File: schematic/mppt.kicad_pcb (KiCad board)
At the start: 2 copper layers, 22 parts, among them J1 Solar, J10 ACS712-OUT, J11 LiIon-36V, J12 Download, J2 TL494-IN, J3 LM2596-IN, J4 LM2596-IN, J5 Serial, J6 LM2596-OUT-4,5V, J7 LM2596-OUT-3,3V, J8 ACS712-IN, J9 TL494-OUT-42V-3A, U3 ESP-03, U4 74HC4051

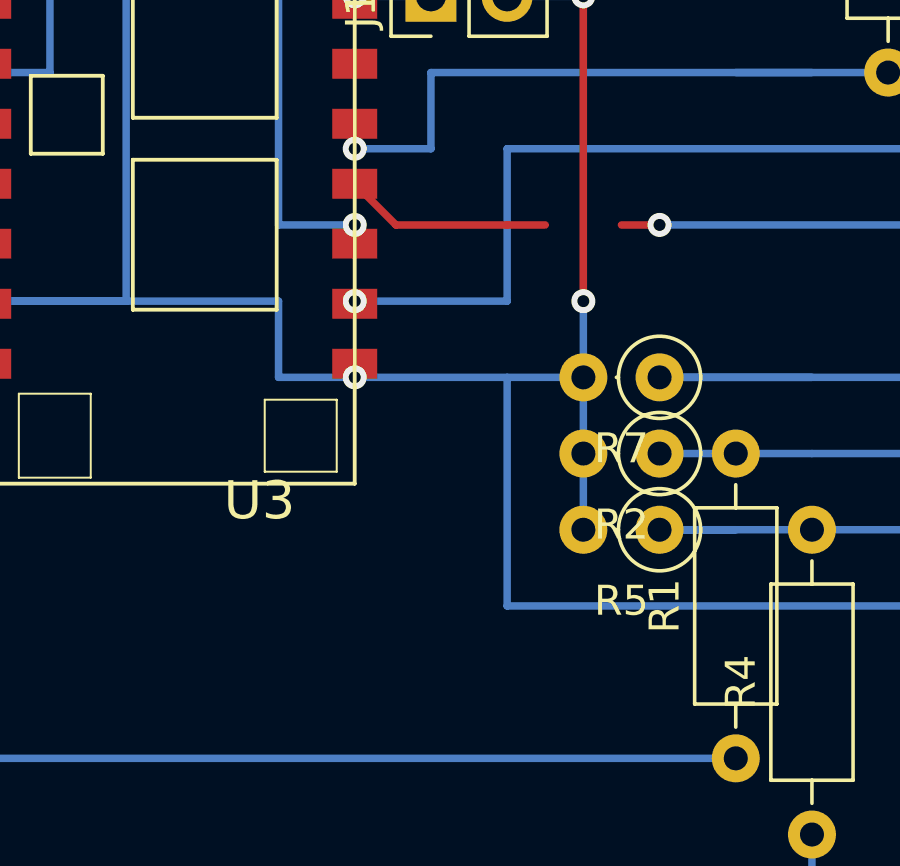
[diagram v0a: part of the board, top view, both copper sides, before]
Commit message: schematic: Use rsistor for DTC connection to limit current to TL494 capacitor
Signed-off-by: Timo Wischer <twischer@freenet.de>
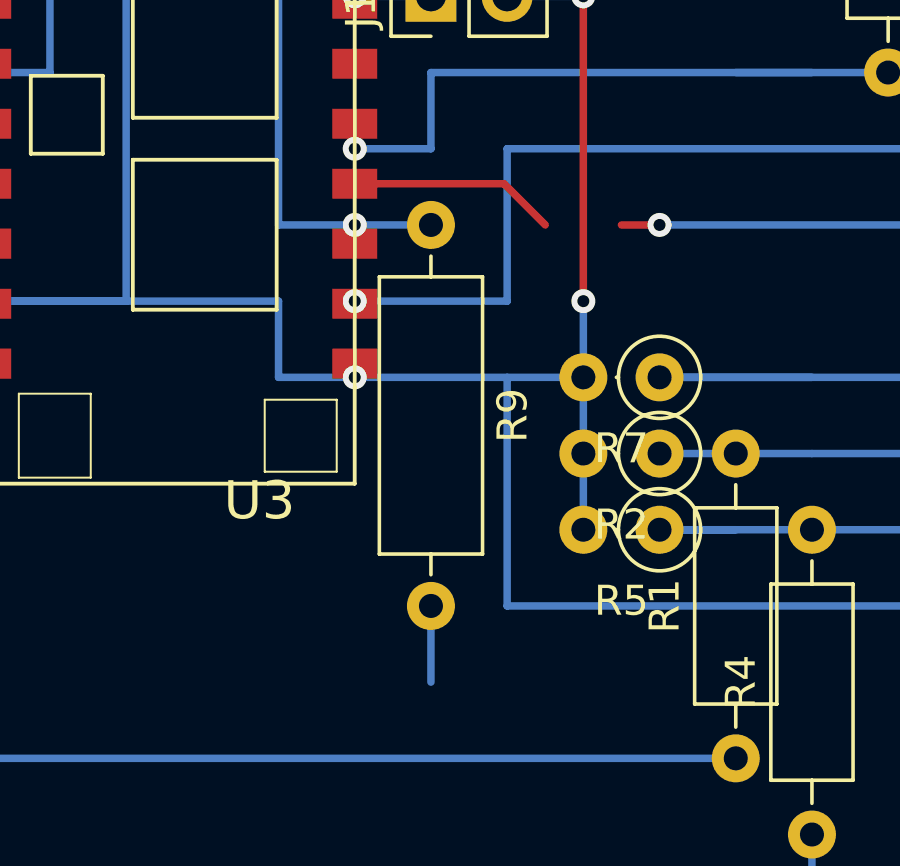
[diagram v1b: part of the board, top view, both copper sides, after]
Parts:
- added R9: 1k2, Resistor_THT:R_Axial_DIN0309_L9.0mm_D3.2mm_P12.70mm_Horizontal, F.Cu at (81.3, 127.0)
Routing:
- net (no net): track 0.00 -> 2.54 mm
- net Net-(D1-Pad1): track 18.4 -> 20.9 mm
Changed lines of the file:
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@@
     (thickness 1.6)
     (drawings 0)
-    (tracks 124)
+    (tracks 125)
     (zones 0)
-    (modules 22)
+    (modules 23)
     (nets 20)
   )
@@
     (uvia_drill 0.1)
     (add_net GND)
+    (add_net "Net-(C1-Pad2)")
     (add_net "Net-(D1-Pad1)")
     (add_net "Net-(J1-Pad2)")
@@
     (add_net "Net-(U4-Pad4)")
     (add_net "Net-(U4-Pad5)")
+  )
+  (module Resistor_THT:R_Axial_DIN0309_L9.0mm_D3.2mm_P12.70mm_Horizontal (layer F.Cu)
+    (at 81.28 127 270)
+    (descr "Resistor, Axial_DIN0309 series, Axial, Horizontal, pin pitch=12.7mm, 0.5W = 1/2W, length*diameter=9*3.2mm^2, http://cdn-reichelt.de/documents/datenblatt/B400/1_4W%23YAG.pdf")
+    (tags "Resistor Axial_DIN0309 series Axial Horizontal pin pitch 12.7mm 0.5W = 1/2W length 9mm diameter 3.2mm")
+    (fp_text reference R9 (at 6.35 -2.72 90) (layer F.SilkS)
+      (effects (font (size 1 1) (thickness 0.15)))
+    )
+    (fp_text value 1k2 (at 6.35 2.72 90) (layer F.Fab)
+      (effects (font (size 1 1) (thickness 0.15)))
+    )
+    (fp_text user %R (at 6.35 0 90) (layer F.Fab)
+      (effects (font (size 1 1) (thickness 0.15)))
+    )
+    (fp_line (start 13.75 -1.85) (end -1.05 -1.85) (layer F.CrtYd) (width 0.05))
+    (fp_line (start 13.75 1.85) (end 13.75 -1.85) (layer F.CrtYd) (width 0.05))
+    (fp_line (start -1.05 1.85) (end 13.75 1.85) (layer F.CrtYd) (width 0.05))
+    (fp_line (start -1.05 -1.85) (end -1.05 1.85) (layer F.CrtYd) (width 0.05))
+    (fp_line (start 11.66 0) (end 10.97 0) (layer F.SilkS) (width 0.12))
+    (fp_line (start 1.04 0) (end 1.73 0) (layer F.SilkS) (width 0.12))
+    (fp_line (start 10.97 -1.72) (end 1.73 -1.72) (layer F.SilkS) (width 0.12))
+    (fp_line (start 10.97 1.72) (end 10.97 -1.72) (layer F.SilkS) (width 0.12))
+    (fp_line (start 1.73 1.72) (end 10.97 1.72) (layer F.SilkS) (width 0.12))
+    (fp_line (start 1.73 -1.72) (end 1.73 1.72) (layer F.SilkS) (width 0.12))
+    (fp_line (start 12.7 0) (end 10.85 0) (layer F.Fab) (width 0.1))
+    (fp_line (start 0 0) (end 1.85 0) (layer F.Fab) (width 0.1))
+    (fp_line (start 10.85 -1.6) (end 1.85 -1.6) (layer F.Fab) (width 0.1))
+    (fp_line (start 10.85 1.6) (end 10.85 -1.6) (layer F.Fab) (width 0.1))
+    (fp_line (start 1.85 1.6) (end 10.85 1.6) (layer F.Fab) (width 0.1))
+    (fp_line (start 1.85 -1.6) (end 1.85 1.6) (layer F.Fab) (width 0.1))
+    (pad 2 thru_hole oval (at 12.7 0 270) (size 1.6 1.6) (drill 0.8) (layers *.Cu *.Mask))
+    (pad 1 thru_hole circle (at 0 0 270) (size 1.6 1.6) (drill 0.8) (layers *.Cu *.Mask)
+      (net 11 "Net-(D1-Pad1)"))
+    (model ${KISYS3DMOD}/Resistor_THT.3dshapes/R_Axial_DIN0309_L9.0mm_D3.2mm_P12.70mm_Horizontal.wrl
+      (at (xyz 0 0 0))
+      (scale (xyz 1 1 1))
+      (rotate (xyz 0 0 0))
+    )
   )
   (module Diode_THT:D_DO-15_P2.54mm_Vertical_AnodeUp (layer F.Cu)
@@
     )
   )
-  (via (at 78.74 129.54) (size 0.8) (drill 0.4) (layers F.Cu B.Cu) (net 17))
-  (segment (start 78.74 129.54) (end 78.74 129.87908) (width 0.25) (layer F.Cu) (net 17))
-  (segment (start 83.82 129.54) (end 78.74 129.54) (width 0.25) (layer B.Cu) (net 17))
-  (segment (start 83.82 124.46) (end 83.82 129.54) (width 0.25) (layer B.Cu) (net 17))
-  (segment (start 80.11288 127) (end 78.74 125.62712) (width 0.25) (layer F.Cu) (net 18))
-  (via (at 88.9 127) (size 0.8) (drill 0.4) (layers F.Cu B.Cu) (net 18))
+  (segment (start 81.28 139.7) (end 81.28 142.24) (width 0.25) (layer B.Cu) (net 0))
   (segment (start 106.68 127) (end 106.68 124.46) (width 0.25) (layer B.Cu) (net 1))
   (segment (start 106.68 124.46) (end 106.68 121.92) (width 0.25) (layer B.Cu) (net 1))
@@
   (segment (start 66.54 123.96) (end 66.04 124.46) (width 0.25) (layer F.Cu) (net 10))
   (segment (start 63.5 124.46) (end 66.04 124.46) (width 0.25) (layer B.Cu) (net 10))
+  (segment (start 76.2 116.84) (end 76.2 127) (width 0.25) (layer B.Cu) (net 11))
+  (segment (start 76.2 127) (end 78.74 127) (width 0.25) (layer B.Cu) (net 11))
+  (via (at 78.74 127) (size 0.8) (drill 0.4) (layers F.Cu B.Cu) (net 11))
+  (segment (start 78.74 127) (end 78.74 127.62356) (width 0.25) (layer F.Cu) (net 11))
+  (segment (start 81.28 116.84) (end 76.2 116.84) (width 0.25) (layer B.Cu) (net 11))
+  (segment (start 81.28 127) (end 78.74 127) (width 0.25) (layer B.Cu) (net 11))
+  (segment (start 60.96 124.46) (end 60.96 127) (width 0.25) (layer B.Cu) (net 12))
+  (via (at 60.96 127) (size 0.8) (drill 0.4) (layers F.Cu B.Cu) (net 12))
+  (segment (start 65.16712 127) (end 66.54 125.62712) (width 0.25) (layer F.Cu) (net 12))
+  (segment (start 60.96 127) (end 65.16712 127) (width 0.25) (layer F.Cu) (net 12))
+  (via (at 66.04 121.92) (size 0.8) (drill 0.4) (layers F.Cu B.Cu) (net 13))
+  (segment (start 66.24662 121.92) (end 66.54 121.62662) (width 0.25) (layer F.Cu) (net 13))
+  (segment (start 66.04 121.92) (end 66.24662 121.92) (width 0.25) (layer F.Cu) (net 13))
+  (segment (start 68.58 121.92) (end 66.04 121.92) (width 0.25) (layer B.Cu) (net 13))
+  (segment (start 106.68 134.62) (end 104.14 134.62) (width 0.25) (layer B.Cu) (net 13))
+  (segment (start 104.14 134.62) (end 104.14 114.3) (width 0.25) (layer B.Cu) (net 13))
+  (segment (start 68.58 121.92) (end 68.58 114.3) (width 0.25) (layer B.Cu) (net 13))
+  (segment (start 68.58 114.3) (end 104.14 114.3) (width 0.25) (layer B.Cu) (net 13))
   (segment (start 78.74 131.62406) (end 78.74 132.08) (width 0.25) (layer F.Cu) (net 15))
   (via (at 78.74 132.08) (size 0.8) (drill 0.4) (layers F.Cu B.Cu) (net 15))
@@
   (segment (start 66.04 129.54) (end 76.2 129.54) (width 0.25) (layer B.Cu) (net 15))
   (segment (start 76.2 129.54) (end 76.2 132.08) (width 0.25) (layer B.Cu) (net 15))
-  (via (at 66.04 121.92) (size 0.8) (drill 0.4) (layers F.Cu B.Cu) (net 13))
-  (segment (start 66.24662 121.92) (end 66.54 121.62662) (width 0.25) (layer F.Cu) (net 13))
-  (segment (start 66.04 121.92) (end 66.24662 121.92) (width 0.25) (layer F.Cu) (net 13))
-  (segment (start 68.58 121.92) (end 66.04 121.92) (width 0.25) (layer B.Cu) (net 13))
-  (segment (start 106.68 134.62) (end 104.14 134.62) (width 0.25) (layer B.Cu) (net 13))
-  (segment (start 104.14 134.62) (end 104.14 114.3) (width 0.25) (layer B.Cu) (net 13))
-  (segment (start 76.2 116.84) (end 76.2 127) (width 0.25) (layer B.Cu) (net 11))
-  (segment (start 76.2 127) (end 78.74 127) (width 0.25) (layer B.Cu) (net 11))
-  (via (at 78.74 127) (size 0.8) (drill 0.4) (layers F.Cu B.Cu) (net 11))
-  (segment (start 78.74 127) (end 78.74 127.62356) (width 0.25) (layer F.Cu) (net 11))
-  (segment (start 81.28 116.84) (end 76.2 116.84) (width 0.25) (layer B.Cu) (net 11))
-  (segment (start 60.96 124.46) (end 60.96 127) (width 0.25) (layer B.Cu) (net 12))
-  (via (at 60.96 127) (size 0.8) (drill 0.4) (layers F.Cu B.Cu) (net 12))
-  (segment (start 65.16712 127) (end 66.54 125.62712) (width 0.25) (layer F.Cu) (net 12))
-  (segment (start 60.96 127) (end 65.16712 127) (width 0.25) (layer F.Cu) (net 12))
-  (segment (start 68.58 121.92) (end 68.58 114.3) (width 0.25) (layer B.Cu) (net 13))
-  (segment (start 68.58 114.3) (end 104.14 114.3) (width 0.25) (layer B.Cu) (net 13))
   (segment (start 66.04 129.54) (end 71.12 129.54) (width 0.25) (layer B.Cu) (net 15))
   (segment (start 71.12 129.54) (end 71.12 116.84) (width 0.25) (layer B.Cu) (net 15))
@@
   (segment (start 78.74 119.38) (end 78.74 119.62764) (width 0.25) (layer F.Cu) (net 16))
   (segment (start 81.28 119.38) (end 78.74 119.38) (width 0.25) (layer B.Cu) (net 16))
+  (via (at 78.74 129.54) (size 0.8) (drill 0.4) (layers F.Cu B.Cu) (net 17))
+  (segment (start 78.74 129.54) (end 78.74 129.87908) (width 0.25) (layer F.Cu) (net 17))
+  (segment (start 83.82 129.54) (end 78.74 129.54) (width 0.25) (layer B.Cu) (net 17))
+  (segment (start 83.82 124.46) (end 83.82 129.54) (width 0.25) (layer B.Cu) (net 17))
   (segment (start 99.06 124.46) (end 83.82 124.46) (width 0.25) (layer B.Cu) (net 17))
+  (via (at 88.9 127) (size 0.8) (drill 0.4) (layers F.Cu B.Cu) (net 18))
   (segment (start 99.06 127) (end 88.9 127) (width 0.25) (layer B.Cu) (net 18))
-  (segment (start 80.11288 127) (end 83.82 127) (width 0.25) (layer F.Cu) (net 18))
-  (segment (start 83.82 127) (end 85.09 127) (width 0.25) (layer F.Cu) (net 18))
   (segment (start 88.9 127) (end 87.63 127) (width 0.25) (layer F.Cu) (net 18))
+  (segment (start 78.74 125.62712) (end 83.71712 125.62712) (width 0.25) (layer F.Cu) (net 18))
+  (segment (start 83.71712 125.62712) (end 85.09 127) (width 0.25) (layer F.Cu) (net 18))
 )

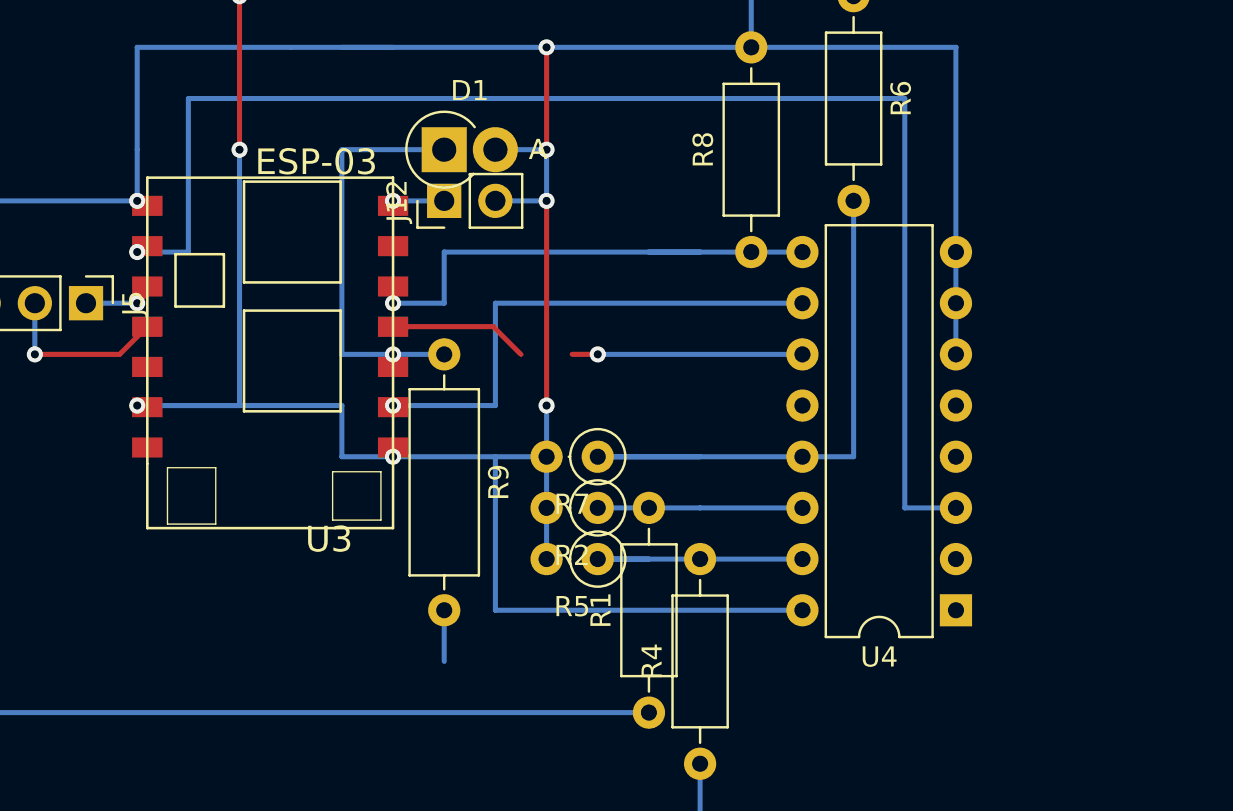
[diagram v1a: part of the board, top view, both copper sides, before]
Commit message: schematic: Add 100nF capacitors
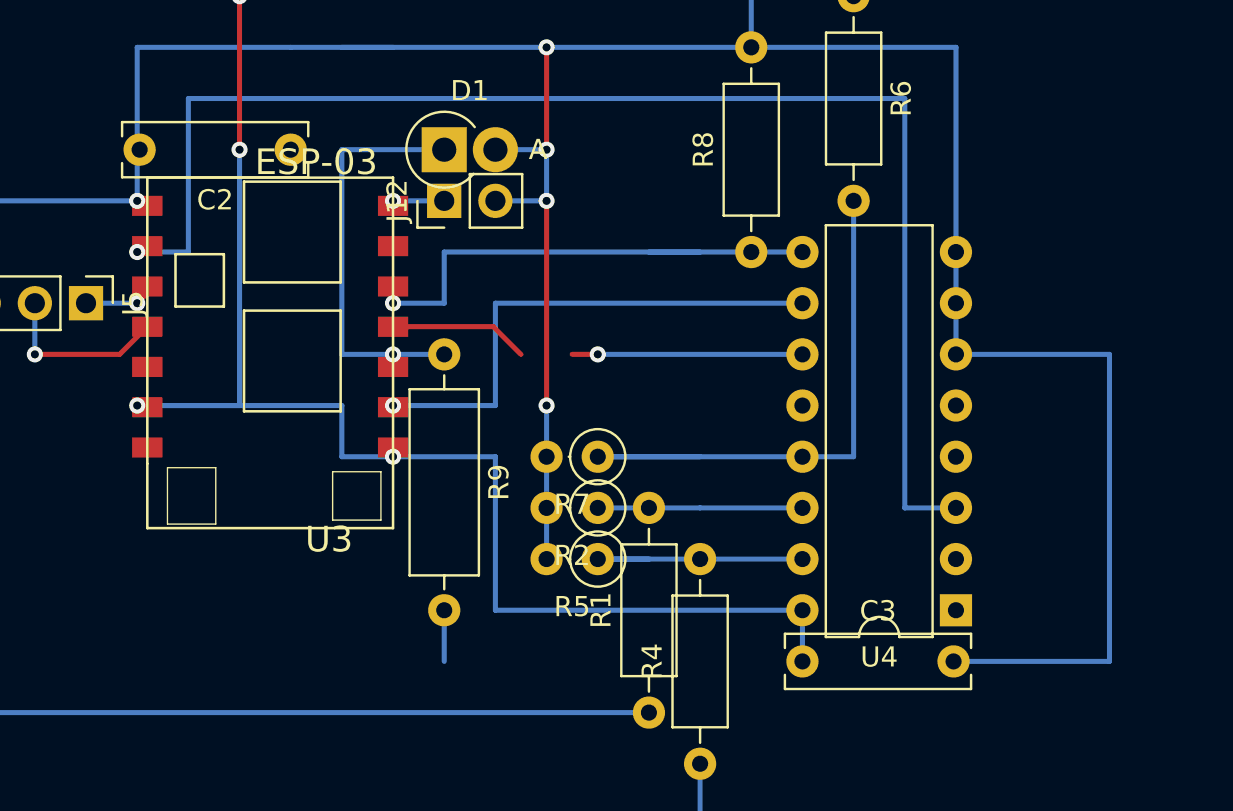
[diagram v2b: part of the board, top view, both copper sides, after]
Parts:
- added C2: 100n, Capacitor_THT:C_Rect_L9.0mm_W2.5mm_P7.50mm_MKT, F.Cu at (73.7, 116.8)
- added C3: 100n, Capacitor_THT:C_Rect_L9.0mm_W2.5mm_P7.50mm_MKT, F.Cu at (99.1, 142.2)
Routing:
- net GND: track 208.9 -> 239.5 mm
